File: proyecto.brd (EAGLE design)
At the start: 95.8 x 48.2 mm, 0 parts

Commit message: Avance :)
.
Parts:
- added IC1: ADE9153AACPZ, SamacSys_Parts:QFN50P500X500X80-33N
- added J1: 796638-3, SamacSys_Parts:SHDRRA3W102P0X508_1X3_1706X120
- added K1: PR28-3V-360-1A-E, PR28-3V-360-1A-E:RELAY_PR28-3V-360-1A-E
- added PS1: RAC03-3.3SK, SamacSys_Parts:RAC0305SK
- added U1: ESP32-PICO-MINI-02-N8R2ESP32-PICO-MINI-02_EXP, 2024-09-07_16-09-34_Library:ESP32-PICO-MINI-02_EXP
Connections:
- new net 3V3: U1.3
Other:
- outline, holes or cut-outs redrawn
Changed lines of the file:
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@@
 <wire x1="36.7538" y1="4.826" x2="36.7538" y2="7.1628" width="0.1524" layer="20"/>
 <wire x1="36.7538" y1="7.1628" x2="44.6786" y2="7.1628" width="0.1524" layer="20"/>
-<wire x1="40.7162" y1="-7.1628" x2="36.7538" y2="-7.1628" width="0.1524" layer="20"/>
 <wire x1="36.7538" y1="-7.1628" x2="36.7538" y2="-4.826" width="0.1524" layer="20"/>
 <wire x1="36.7538" y1="-4.826" x2="44.6786" y2="-4.826" width="0.1524" layer="20"/>
 <wire x1="44.6786" y1="-4.826" x2="44.6786" y2="-7.1628" width="0.1524" layer="20"/>
-<wire x1="44.6786" y1="-7.1628" x2="40.7162" y2="-7.1628" width="0.1524" layer="20"/>
+<wire x1="44.6786" y1="-7.1628" x2="36.7538" y2="-7.1628" width="0.1524" layer="20"/>
 <circle x="28.7782" y="0" radius="3.2131" width="0.1524" layer="20"/>
+<circle x="-36.576" y="20.2692" radius="2.54" width="0" layer="29"/>
+<circle x="36.576" y="20.2692" radius="2.54" width="0" layer="29"/>
+<circle x="36.576" y="-20.2692" radius="2.54" width="0" layer="29"/>
+<circle x="-36.576" y="-20.2692" radius="2.54" width="0" layer="29"/>
 </plain>
 <attributes>
@@
 </autorouter>
 <elements>
+<element name="J1" library="SamacSys_Parts" package="SHDRRA3W102P0X508_1X3_1706X120" value="796638-3" x="-41.91" y="11.43" smashed="yes" rot="R90">
+<attribute name="DESCRIPTION" value="Body Features: Primary Product Color Green | Product Orientation Right Angle | Configuration Features: Stacking Configuration Side Stackable | Number of Positions 3 | Number of Rows 1 | Contact Features: Contact Base Material Phosphor Bronze | Contact Current Rating (Max) 15 AMP | Contact Mating Area Plating Material Tin | Dimensions: Wire Size .05  3 MMSQ | Wire Size 30  12 AWG | Electrical Characteristics: Operating Voltage 300 VAC | Housing Features: Housing Material PA 66 | Centerline (Pitch) .2 I" x="-41.91" y="11.43" size="1.778" layer="27" rot="R90" display="off"/>
+<attribute name="HEIGHT" value="8.5mm" x="-41.91" y="11.43" size="1.778" layer="27" rot="R90" display="off"/>
+<attribute name="MANUFACTURER_NAME" value="TE Connectivity" x="-41.91" y="11.43" size="1.778" layer="27" rot="R90" display="off"/>
+<attribute name="MANUFACTURER_PART_NUMBER" value="796638-3" x="-41.91" y="11.43" size="1.778" layer="27" rot="R90" display="off"/>
+<attribute name="MOUSER_PART_NUMBER" value="571-7966383" x="-41.91" y="11.43" size="1.778" layer="27" rot="R90" display="off"/>
+<attribute name="MOUSER_PRICE-STOCK" value="https://www.mouser.co.uk/ProductDetail/TE-Connectivity/796638-3?qs=OgP1KchuM4OaLB9LUcSrBQ%3D%3D" x="-41.91" y="11.43" size="1.778" layer="27" rot="R90" display="off"/>
+<attribute name="NAME" x="-44.45" y="10.16" size="1.27" layer="25" rot="R90" align="center"/>
+<attribute name="VALUE" x="-44.45" y="2.54" size="1.27" layer="27" rot="R90" align="center"/>
+</element>
+<element name="PS1" library="SamacSys_Parts" package="RAC0305SK" value="RAC03-3.3SK" x="21.59" y="0" smashed="yes" rot="R180">
+<attribute name="DESCRIPTION" value="AC/DC Power Modules 3W 85-264Vin 3.3Vout 900mA" x="21.59" y="0" size="1.778" layer="27" rot="R180" display="off"/>
+<attribute name="HEIGHT" value="18.4mm" x="21.59" y="0" size="1.778" layer="27" rot="R180" display="off"/>
+<attribute name="MANUFACTURER_NAME" value="RECOM Power" x="21.59" y="0" size="1.778" layer="27" rot="R180" display="off"/>
+<attribute name="MANUFACTURER_PART_NUMBER" value="RAC03-3.3SK" x="21.59" y="0" size="1.778" layer="27" rot="R180" display="off"/>
+<attribute name="MOUSER_PART_NUMBER" value="919-RAC03-3.3SK" x="21.59" y="0" size="1.778" layer="27" rot="R180" display="off"/>
+<attribute name="MOUSER_PRICE-STOCK" value="https://www.mouser.co.uk/ProductDetail/RECOM-Power/RAC03-3.3SK?qs=EBDBlbfErPyS11fagCV%252BCw%3D%3D" x="21.59" y="0" size="1.778" layer="27" rot="R180" display="off"/>
+<attribute name="NAME" x="11.135" y="-11.43" size="1.27" layer="25" rot="R180" align="center"/>
+<attribute name="VALUE" x="9.865" y="-3.81" size="1.27" layer="27" rot="R180" align="center"/>
+</element>
+<element name="K1" library="PR28-3V-360-1A-E" package="RELAY_PR28-3V-360-1A-E" value="PR28-3V-360-1A-E" x="-26.3906" y="-9.2202" smashed="yes" rot="R180">
+<attribute name="AVAILABILITY" value="In Stock" x="-26.3906" y="-9.2202" size="1.778" layer="27" rot="R180" display="off"/>
+<attribute name="CHECK_PRICES" value="https://www.snapeda.com/parts/PR28-3V-360-1A-E/Same+Sky/view-part/?ref=eda" x="-26.3906" y="-9.2202" size="1.778" layer="27" rot="R180" display="off"/>
+<attribute name="CUI_PURCHASE_URL" value="https://www.cuidevices.com/product/relays/power-relays/pr28-3v-360-1a-e?utm_source=snapeda.com&amp;utm_medium=referral&amp;utm_campaign=snapedaBOM" x="-26.3906" y="-9.2202" size="1.778" layer="27" rot="R180" display="off"/>
+<attribute name="DESCRIPTION" value="22 x 16 x 16.6 mm, 3 V, 16 A, SPST (1 Form A), Epoxy Sealed, Class F, Power Relay" x="-26.3906" y="-9.2202" size="1.778" layer="27" rot="R180" display="off"/>
+<attribute name="MF" value="CUI Devices" x="-26.3906" y="-9.2202" size="1.778" layer="27" rot="R180" display="off"/>
+<attribute name="MP" value="PR28-3V-360-1A-E" x="-26.3906" y="-9.2202" size="1.778" layer="27" rot="R180" display="off"/>
+<attribute name="NAME" x="-18.1806" y="-12.1202" size="1.27" layer="25" rot="R180"/>
+<attribute name="PACKAGE" value="None" x="-26.3906" y="-9.2202" size="1.778" layer="27" rot="R180" display="off"/>
+<attribute name="PRICE" value="None" x="-26.3906" y="-9.2202" size="1.778" layer="27" rot="R180" display="off"/>
+<attribute name="PURCHASE-URL" value="https://www.snapeda.com/api/url_track_click_mouser/?unipart_id=15935205&amp;manufacturer=CUI Devices&amp;part_name=PR28-3V-360-1A-E&amp;search_term=None" x="-26.3906" y="-9.2202" size="1.778" layer="27" rot="R180" display="off"/>
+<attribute name="SNAPEDA_LINK" value="https://www.snapeda.com/parts/PR28-3V-360-1A-E/Same+Sky/view-part/?ref=snap" x="-26.3906" y="-9.2202" size="1.778" layer="27" rot="R180" display="off"/>
+<attribute name="VALUE" x="-21.9906" y="-12.6702" size="1.27" layer="27" rot="R180" align="top-left"/>
+</element>
+<element name="U1" library="2024-09-07_16-09-34_Library" package="ESP32-PICO-MINI-02_EXP" value="ESP32-PICO-MINI-02-N8R2ESP32-PICO-MINI-02_EXP" x="3.81" y="15.5956" smashed="yes">
+<attribute name="COPYRIGHT" value="Copyright (C) 2024 Ultra Librarian. All rights reserved." x="3.81" y="15.5956" size="1.778" layer="27" display="off"/>
+<attribute name="MANUFACTURER_PART_NUMBER" value="ESP32-PICO-MINI-02-N8R2" x="3.81" y="15.5956" size="1.778" layer="27" display="off"/>
+<attribute name="MFR_NAME" value="Espressif Systems" x="3.81" y="15.5956" size="1.778" layer="27" display="off"/>
+<attribute name="NAME" x="-0.7312" y="9.8806" size="1.27" layer="27" ratio="6"/>
+<attribute name="VALUE" x="-1.7288" y="16.2306" size="1.27" layer="27" ratio="6"/>
+</element>
+<element name="IC1" library="SamacSys_Parts" package="QFN50P500X500X80-33N" value="ADE9153AACPZ" x="-22.86" y="10.16" smashed="yes">
+<attribute name="DESCRIPTION" value="Data Acquisition ADCs/DACs - Specialized 1 PH Mtr IC w/ Auto Calibration" x="-22.86" y="10.16" size="1.778" layer="27" display="off"/>
+<attribute name="HEIGHT" value="0.8mm" x="-22.86" y="10.16" size="1.778" layer="27" display="off"/>
+<attribute name="MANUFACTURER_NAME" value="Analog Devices" x="-22.86" y="10.16" size="1.778" layer="27" display="off"/>
+<attribute name="MANUFACTURER_PART_NUMBER" value="ADE9153AACPZ" x="-22.86" y="10.16" size="1.778" layer="27" display="off"/>
+<attribute name="MOUSER_PART_NUMBER" value="584-ADE9153AACPZ" x="-22.86" y="10.16" size="1.778" layer="27" display="off"/>
+<attribute name="MOUSER_PRICE-STOCK" value="https://www.mouser.co.uk/ProductDetail/Analog-Devices/ADE9153AACPZ?qs=rrS6PyfT74fO4%2FDiqnqz3A%3D%3D" x="-22.86" y="10.16" size="1.778" layer="27" display="off"/>
+<attribute name="NAME" x="-17.78" y="10.16" size="1.27" layer="25" align="center"/>
+<attribute name="VALUE" x="-21.59" y="6.35" size="1.27" layer="27" align="center"/>
+</element>
 </elements>
 <signals>
+<signal name="3V3">
+<contactref element="U1" pad="3"/>
+</signal>
 </signals>
 <mfgpreviewcolors>

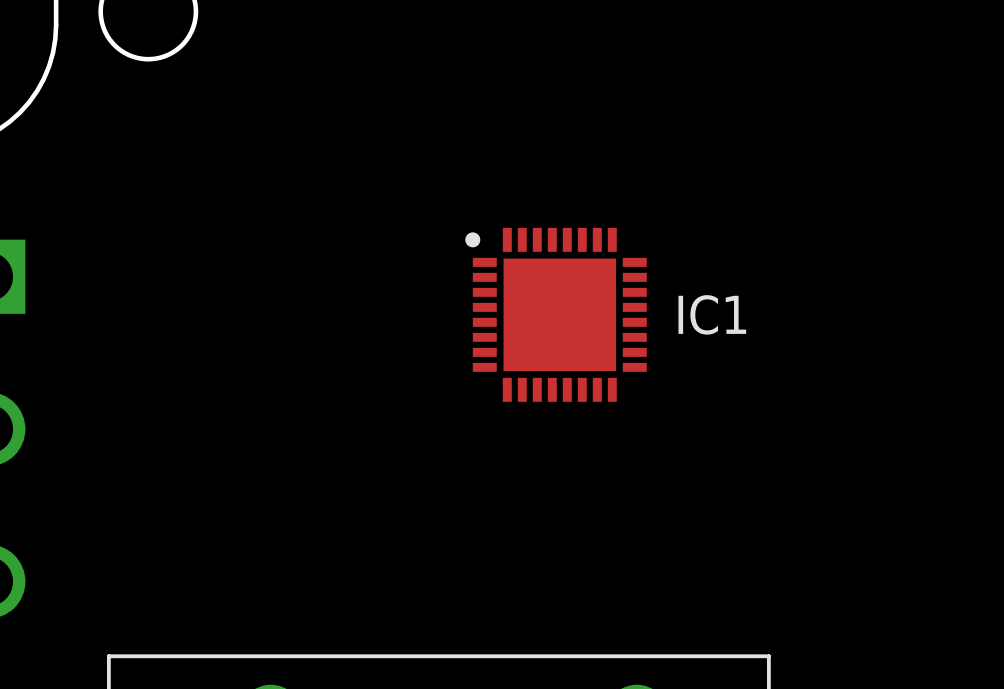
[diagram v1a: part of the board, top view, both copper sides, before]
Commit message: Condensadores de acople del integrado de medicion de energia
Se añadio algunos condensadores de acople que se especifico en la hoja de datos del medidor de energia y el oscilador que se especifica.
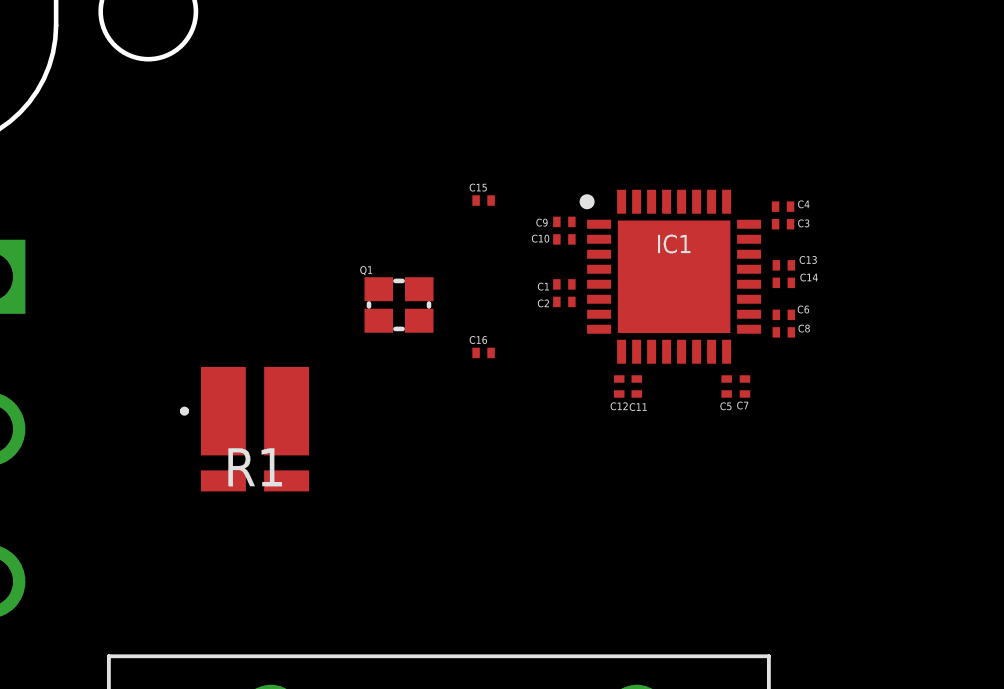
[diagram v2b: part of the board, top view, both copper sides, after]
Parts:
- added C1, C11, C13, C3, C7, C8, C9: 0.1u, rcl:C0201
- added C10, C12, C14, C2, C4, C5, C6: 4.7u, rcl:C0201
- added C15, C16: 22p, rcl:C0201
- added Q1: 12.288p, crystal-geyer_V1_0:2.0X1.6_KX-5
- added R1: WSK12161L000FEB, SamacSys_Parts:WSK12161L000FEB
- moved IC1 4.02 mm to (-19.1, 11.4)
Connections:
- new net AVDDOUT: C5.1, C7.1, IC1.16
- new net DVDDOUT: C10.1, C9.1, IC1.2
- new net GND: C1.2, C10.2, C11.2, C12.2, C13.2, C14.2, C15.2, C16.1, C2.2, C3.2, C4.2, C5.2, C6.1, C7.2, C8.1, C9.2, IC1.1, IC1.17, IC1.20, IC1.9
- new net MSH: C13.1, C14.1, IC1.21
- new net N$2: C15.1, IC1.3, Q1.3
- new net N$3: C16.2, IC1.4, Q1.1
- new net REFIN: C6.2, C8.2, IC1.18
- new net VDD1: C1.1, C2.1, IC1.5
- new net VDD2: C3.1, C4.1, IC1.24
- new net VDDOUT2P5: C11.1, C12.1, IC1.10
